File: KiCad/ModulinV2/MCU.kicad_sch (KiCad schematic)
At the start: 36 parts, among them IC1 STM32F401RET6, IC2 USBLC6-2SC6, J1 USB4105-GF-A, J2 TSM-103-01-T-DV, J3 TSW-104-07-G-S, SW1 SW_Push, SW2 SW_Push

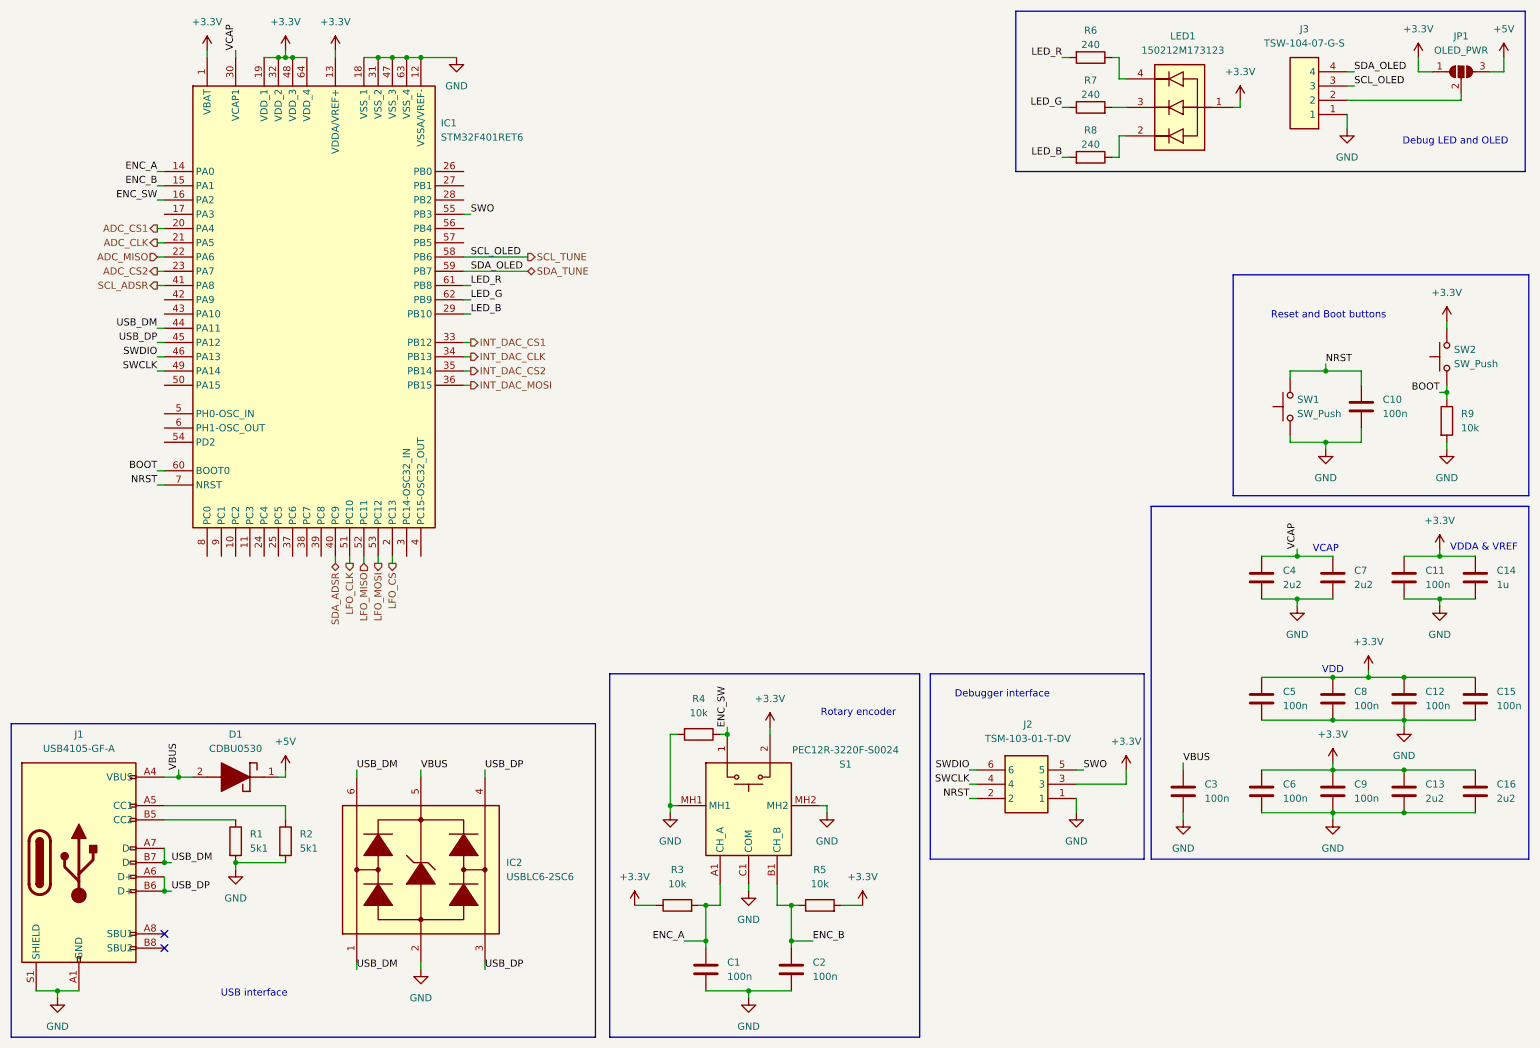
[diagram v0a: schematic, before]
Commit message: Added 4k7 pullups to I2C lines
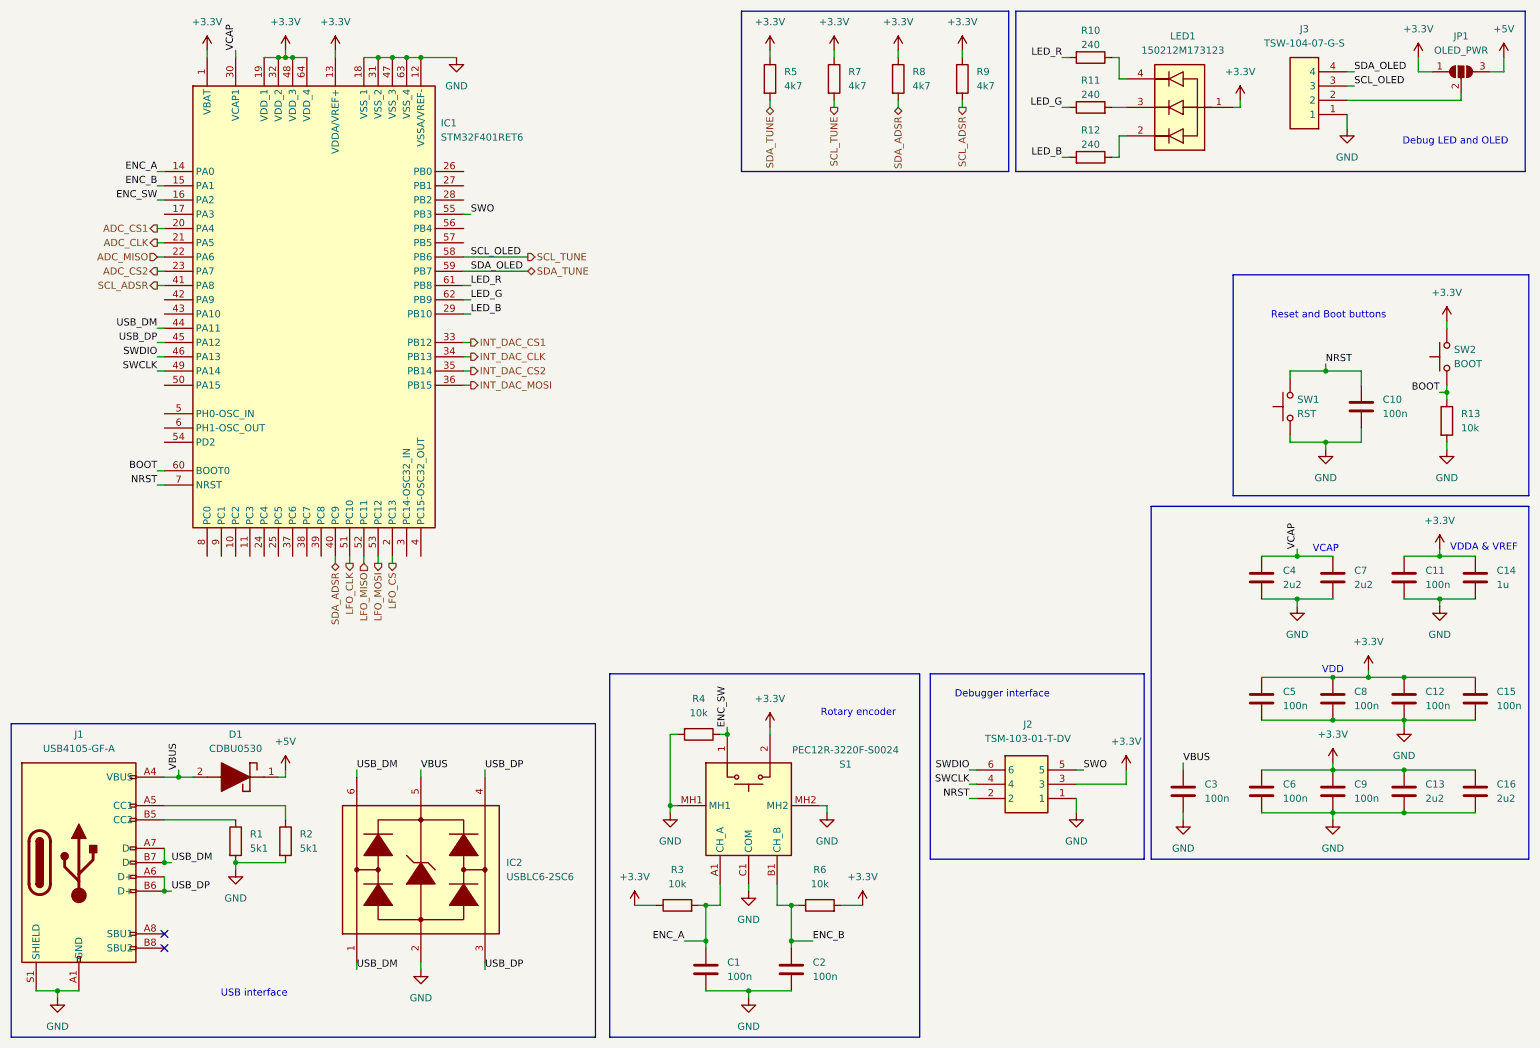
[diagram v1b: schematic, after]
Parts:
- added R5, R7, R8, R9: 4k7, symbol Device:R
- SW1: value SW_Push -> RST
- SW2: value SW_Push -> BOOT
- renumbered R6 to R10, R7 to R11, R8 to R12, R9 to R13, R5 to R6
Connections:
- net +3.3V: now also R5.1, R7.1, R8.1, R9.1
- net SCL_ADSR: now also R9.2
- net SCL_TUNE: now also R7.2
- net SDA_ADSR: now also R8.2
- net SDA_TUNE: now also R5.2

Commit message: Added wave selection jumpers for testing
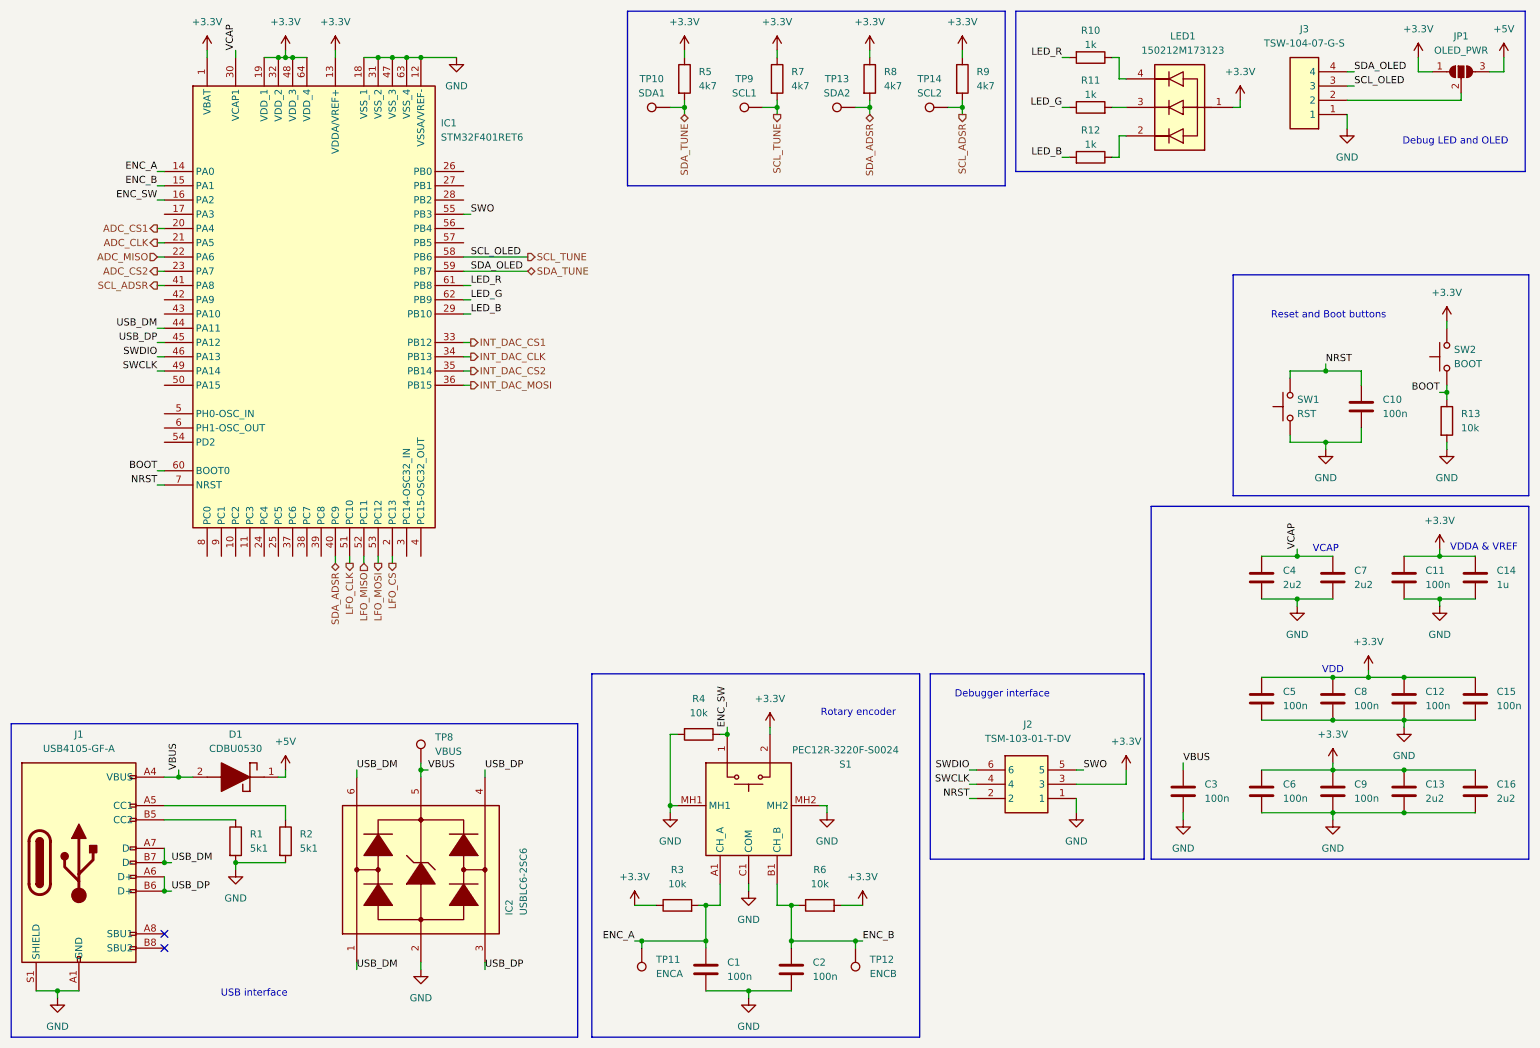
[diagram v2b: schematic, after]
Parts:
- added TP10: SDA1, symbol Connector:TestPoint
- added TP11: ENCA, symbol Connector:TestPoint
- added TP12: ENCB, symbol Connector:TestPoint
- added TP13: SDA2, symbol Connector:TestPoint
- added TP14: SCL2, symbol Connector:TestPoint
- added TP8: VBUS, symbol Connector:TestPoint
- added TP9: SCL1, symbol Connector:TestPoint
- R10, R11, R12: value 240 -> 1k
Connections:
- net ENC_A: now also TP11.1
- net ENC_B: now also TP12.1
- net SCL_ADSR: now also TP14.1
- net SCL_TUNE: now also TP9.1
- net SDA_ADSR: now also TP13.1
- net SDA_TUNE: now also TP10.1
- net VBUS: now also TP8.1
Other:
- moved on the sheet: R5, R7, R8

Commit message: Revert "Modified selection LED schematic and supply caps"
This reverts commit f7ca9d31056dcb2cadf4048ae59e1f5625a2aefa.
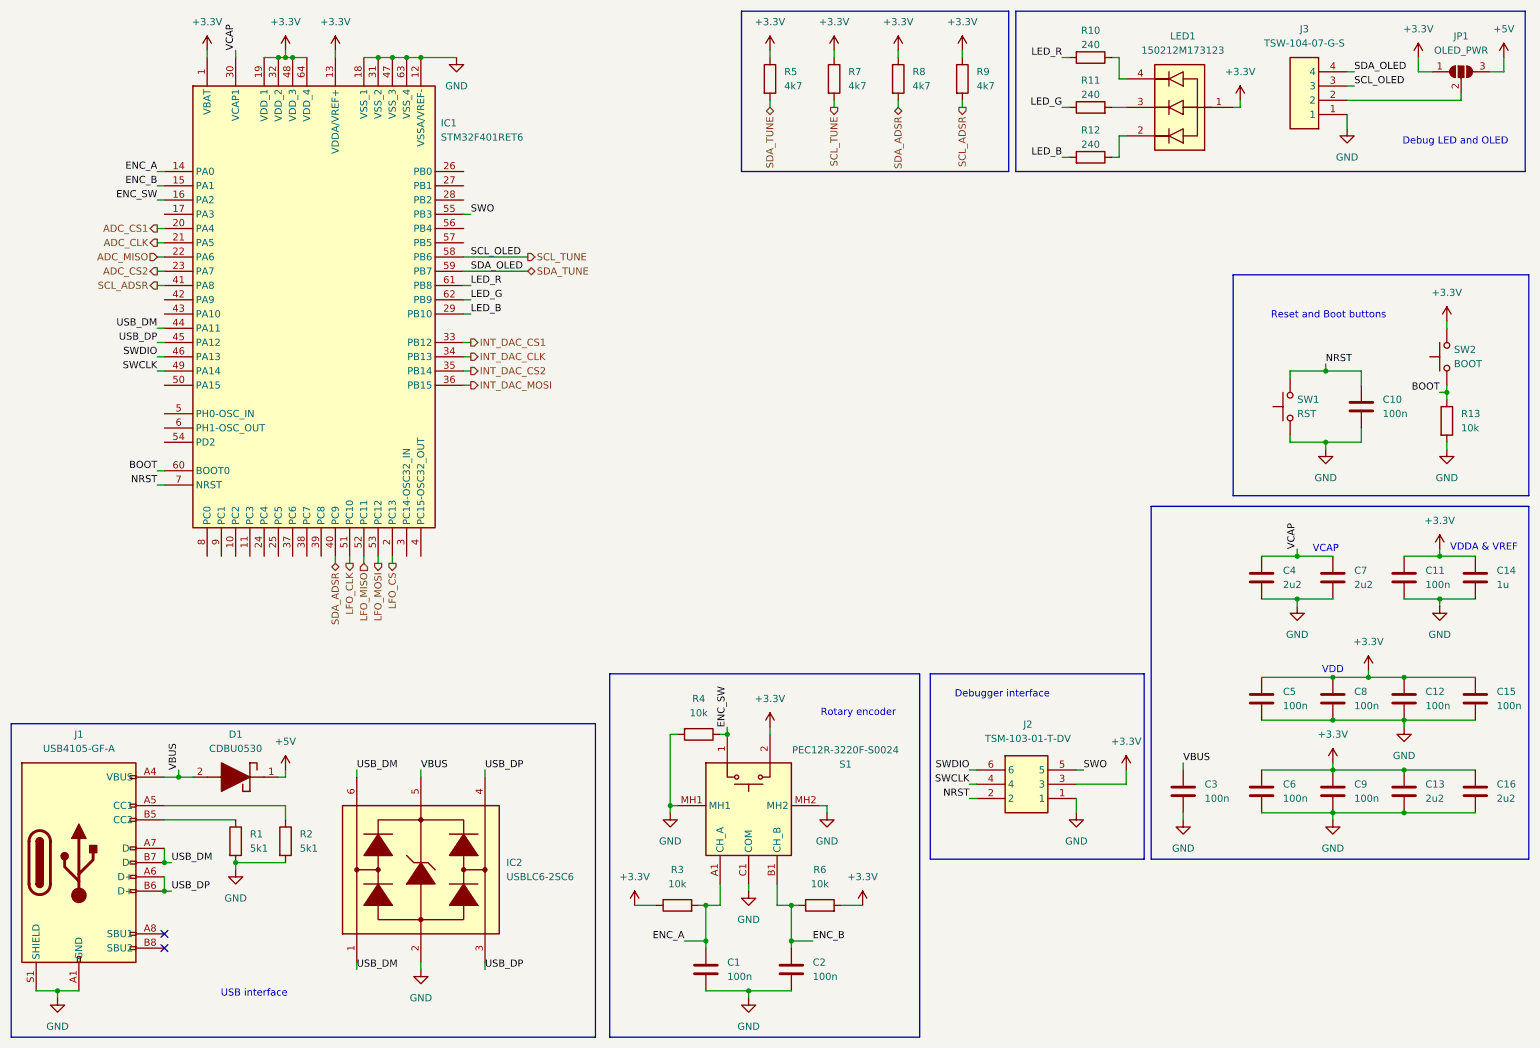
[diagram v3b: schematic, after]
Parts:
- removed TP10: SDA1, symbol Connector:TestPoint
- removed TP11: ENCA, symbol Connector:TestPoint
- removed TP12: ENCB, symbol Connector:TestPoint
- removed TP13: SDA2, symbol Connector:TestPoint
- removed TP14: SCL2, symbol Connector:TestPoint
- removed TP8: VBUS, symbol Connector:TestPoint
- removed TP9: SCL1, symbol Connector:TestPoint
- R10, R11, R12: value 1k -> 240
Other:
- moved on the sheet: R5, R7, R8
